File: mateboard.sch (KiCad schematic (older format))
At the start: 13 parts

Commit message: wifi bt leds
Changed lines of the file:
@@
 Connection ~ 8950 775
 Wire Wire Line
-	8475 775  8550 775
-Wire Wire Line
-	8550 775  8650 775
-Wire Wire Line
-	8650 775  8750 775
-Wire Wire Line
-	8750 775  8850 775
-Wire Wire Line
-	8850 775  8950 775
-Wire Wire Line
-	8950 775  9050 775
-Wire Wire Line
-	9050 775  9150 775
+	8475 775  9150 775
 Wire Wire Line
 	9050 775  9050 900
@@
 	9150 1200 9150 1250
 Wire Wire Line
-	8150 1250 9150 1250
-Wire Wire Line
-	9150 1250 9225 1250
-Wire Wire Line
-	8150 1350 9050 1350
-Wire Wire Line
-	9050 1350 9225 1350
+	8150 1250 9225 1250
+Wire Wire Line
+	8150 1350 9225 1350
 Wire Wire Line
 	9050 1350 9050 1200
 Wire Wire Line
-	8150 1450 8950 1450
-Wire Wire Line
-	8950 1450 9225 1450
+	8150 1450 9225 1450
 Wire Wire Line
 	8950 1450 8950 1200
@@
 	8550 1550 8550 775
 Wire Wire Line
-	8150 1650 8850 1650
-Wire Wire Line
-	8850 1650 9225 1650
+	8150 1650 9225 1650
 Wire Wire Line
 	8850 1650 8850 1200
@@
 $EndComp
 Wire Wire Line
-	9150 1750 9150 2200
-Wire Wire Line
-	9150 2200 9150 2250
+	9150 1750 9150 2250
 Wire Wire Line
 	9150 1750 9225 1750
 Wire Wire Line
-	8150 1850 8750 1850
-Wire Wire Line
-	8750 1850 9225 1850
+	8150 1850 9225 1850
 Wire Wire Line
 	8750 1850 8750 1200
 Wire Wire Line
-	8150 1950 8650 1950
-Wire Wire Line
-	8650 1950 9225 1950
+	8150 1950 9225 1950
 Wire Wire Line
 	8650 1950 8650 1200
@@
 Connection ~ 8550 775
 Wire Wire Line
-	8475 1200 8475 2100
-Wire Wire Line
-	8475 2100 8475 2850
+	8475 1200 8475 2850
 Wire Wire Line
 	9225 2200 9150 2200
@@
 	6500 2850 6275 2850
 Wire Wire Line
-	6275 2400 6275 2850
-Wire Wire Line
-	6275 2850 6275 4650
+	6275 2400 6275 4650
 Wire Wire Line
 	6275 2400 6125 2400

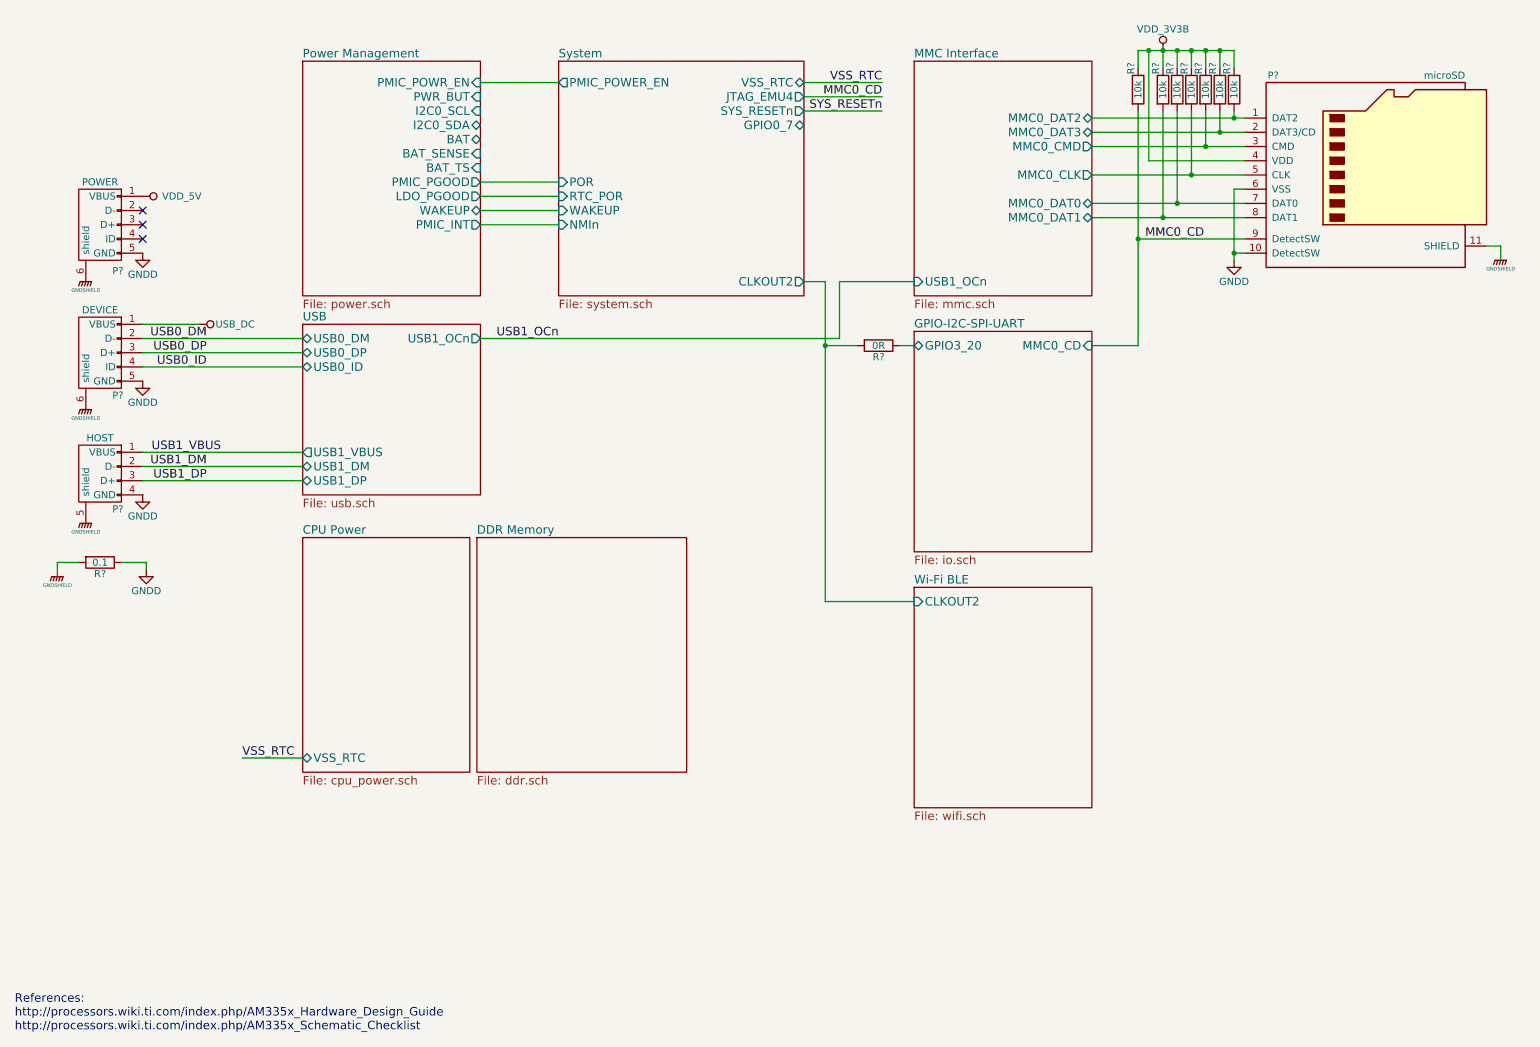
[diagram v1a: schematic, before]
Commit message: id eeprom
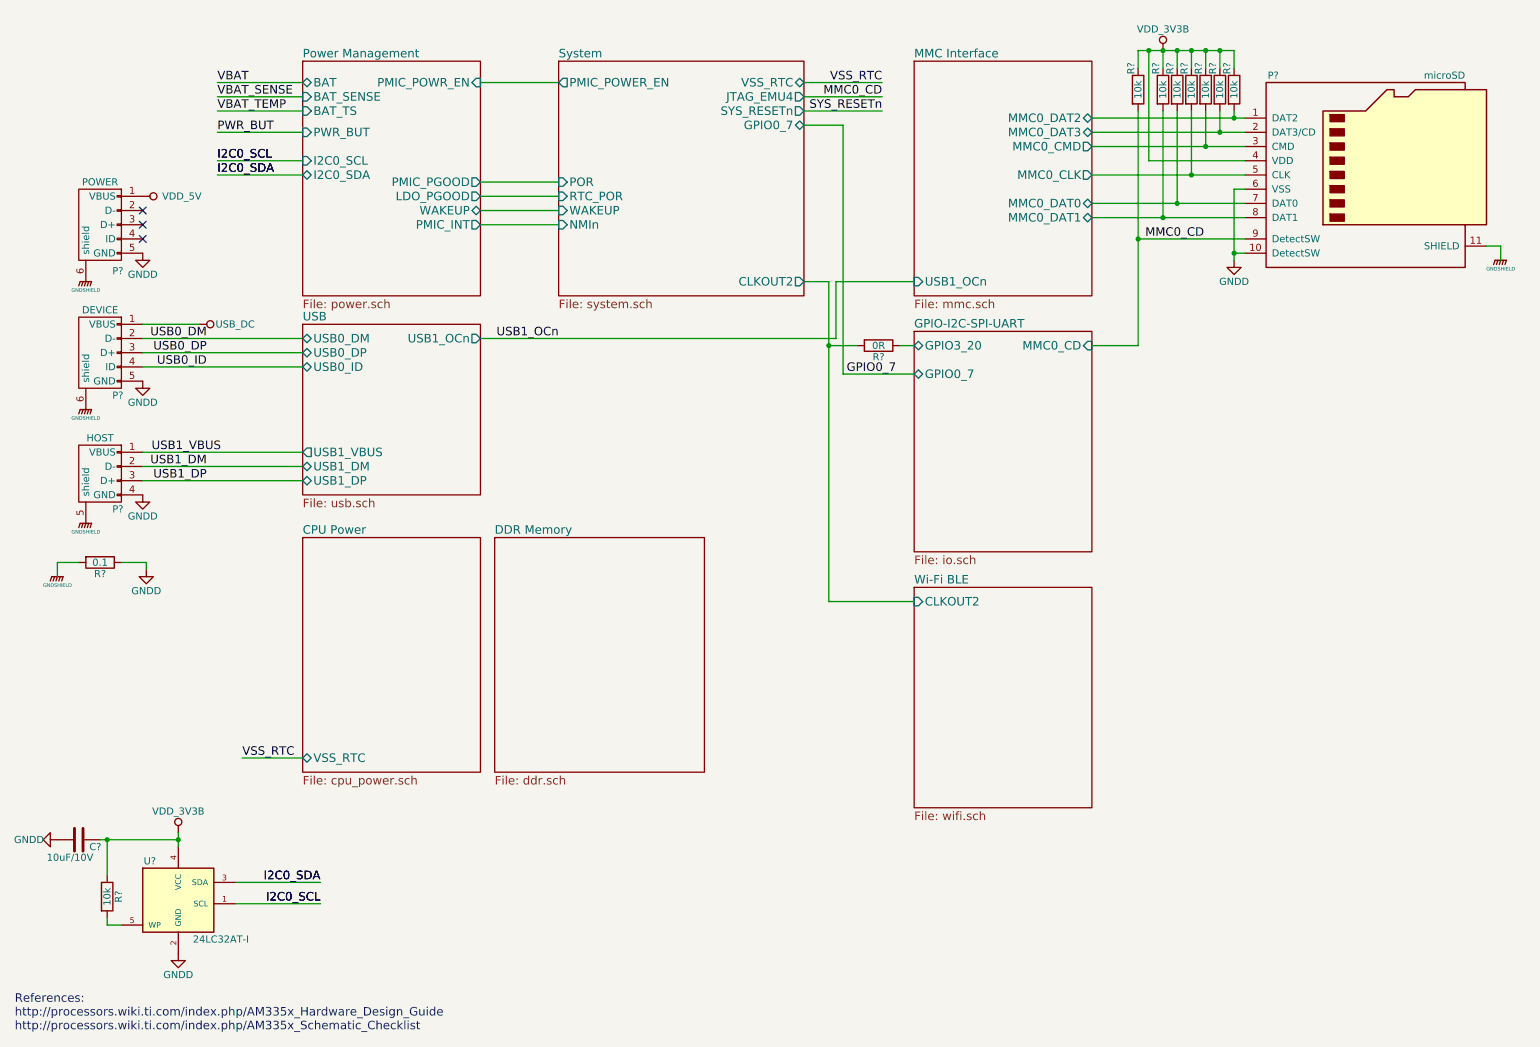
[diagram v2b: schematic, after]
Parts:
- added C?: 10uF/10V, symbol C
- added R?: 10k, symbol R
- added U?: 24LC32AT-I, TO_SOT_Packages_SMD:SOT-23-5, symbol AT24CS32-STUM
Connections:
- net GNDD: now also C?.2, U?.2 (GND)
- net VDD_3V3B: now also C?.1, R?.1, U?.4 (VCC)
- new net: R?.2, U?.5 (WP)
- new net I2C0_SCL: U?.1 (SCL)
- new net I2C0_SDA: U?.3 (SDA)
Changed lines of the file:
@@
 F1 "power.sch" 60
 F2 "PMIC_POWR_EN" I R 3850 1000 60
-F3 "PWR_BUT" I R 3850 1100 60
-F4 "I2C0_SCL" I R 3850 1200 60
-F5 "I2C0_SDA" B R 3850 1300 60
-F6 "BAT" B R 3850 1400 60
-F7 "BAT_SENSE" I R 3850 1500 60
-F8 "BAT_TS" I R 3850 1600 60
+F3 "PWR_BUT" I L 2600 1350 60
+F4 "I2C0_SCL" I L 2600 1550 60
+F5 "I2C0_SDA" B L 2600 1650 60
+F6 "BAT" B L 2600 1000 60
+F7 "BAT_SENSE" I L 2600 1100 60
+F8 "BAT_TS" I L 2600 1200 60
 F9 "PMIC_PGOOD" O R 3850 1700 60
 F10 "LDO_PGOOD" O R 3850 1800 60
@@
 $EndSheet
 $Sheet
-S 3825 4200 1475 1650
+S 3950 4200 1475 1650
 U 589C7F66
 F0 "DDR Memory" 60
@@
 F2 "MMC0_CD" I R 8150 2850 60
 F3 "GPIO3_20" B L 6900 2850 60
+F4 "GPIO0_7" B L 6900 3050 60
 $EndSheet
 $Comp
@@
 	1500 4375 1500 4425
 $Sheet
-S 2600 4200 1175 1650
+S 2600 4200 1250 1650
 U 589E2993
 F0 "CPU Power" 60
@@
 $EndComp
 Wire Wire Line
-	3850 2800 6375 2800
+	3850 2800 6350 2800
 Text Label 4400 2800 2    60   ~ 0
 USB1_OCn
 Wire Wire Line
-	6375 2400 6900 2400
+	6350 2400 6900 2400
 $Sheet
 S 6900 4550 1250 1550
@@
 $EndSheet
 Wire Wire Line
-	6375 2800 6375 2400
+	6350 2800 6350 2400
 Wire Wire Line
 	4400 2000 3850 2000
@@
 	6800 2850 6900 2850
 Wire Wire Line
-	6500 2850 6275 2850
-Wire Wire Line
-	6275 2400 6275 4650
-Wire Wire Line
-	6275 2400 6125 2400
-Wire Wire Line
-	6275 4650 6900 4650
-Connection ~ 6275 2850
+	6500 2850 6300 2850
+Wire Wire Line
+	6300 2400 6300 4650
+Wire Wire Line
+	6300 2400 6125 2400
+Wire Wire Line
+	6300 4650 6900 4650
+Connection ~ 6300 2850
+Wire Wire Line
+	6125 1300 6400 1300
+Wire Wire Line
+	6400 1300 6400 3050
+Wire Wire Line
+	6400 3050 6900 3050
+Text Label 6425 3050 0    60   ~ 0
+GPIO0_7
+Wire Wire Line
+	2600 1000 2000 1000
+Text Label 2000 1000 0    60   ~ 0
+VBAT
+Text Label 2000 1100 0    60   ~ 0
+VBAT_SENSE
+Wire Wire Line
+	2000 1100 2600 1100
+Wire Wire Line
+	2600 1200 2000 1200
+Text Label 2000 1200 0    60   ~ 0
+VBAT_TEMP
+Wire Wire Line
+	2600 1350 2000 1350
+Text Label 2000 1350 0    60   ~ 0
+PWR_BUT
+Wire Wire Line
+	2600 1550 2000 1550
+Wire Wire Line
+	2000 1650 2600 1650
+Text Label 2000 1650 0    60   ~ 0
+I2C0_SDA
+Text Label 2000 1550 0    60   ~ 0
+I2C0_SCL
+$Comp
+L AT24CS32-STUM U?
+U 1 1 58BAF6FC
+P 1725 6725
+F 0 "U?" H 1525 6975 50  0000 C CNN
+F 1 "24LC32AT-I" H 2025 6425 50  0000 C CNN
+F 2 "TO_SOT_Packages_SMD:SOT-23-5" H 1725 6725 50  0001 C CIN
+F 3 "" H 1725 6725 50  0001 C CNN
+	1    1725 6725
+	1    0    0    -1
+$EndComp
+$Comp
+L VDD_3V3B #PWR?
+U 1 1 58BAF78B
+P 1725 6275
+F 0 "#PWR?" H 1725 6125 50  0001 C CNN
+F 1 "VDD_3V3B" H 1725 6425 50  0000 C CNN
+F 2 "" H 1725 6275 50  0000 C CNN
+F 3 "" H 1725 6275 50  0000 C CNN
+	1    1725 6275
+	1    0    0    -1
+$EndComp
+$Comp
+L C C?
+U 1 1 58BB10E1
+P 1025 6325
+F 0 "C?" V 1075 6400 50  0000 L CNN
+F 1 "10uF/10V" V 1150 6100 50  0000 L CNN
+F 2 "" H 1063 6175 50  0000 C CNN
+F 3 "" H 1025 6325 50  0000 C CNN
+	1    1025 6325
+	0    1    1    0
+$EndComp
+$Comp
+L GNDD #PWR?
+U 1 1 58BB10E8
+P 875 6325
+F 0 "#PWR?" H 875 6075 50  0001 C CNN
+F 1 "GNDD" V 875 6125 50  0000 C CNN
+F 2 "" H 875 6325 50  0000 C CNN
+F 3 "" H 875 6325 50  0000 C CNN
+	1    875  6325
+	0    1    1    0
+$EndComp
+Wire Wire Line
+	1175 6325 1725 6325
+Wire Wire Line
+	1725 6275 1725 6375
+Connection ~ 1725 6325
+$Comp
+L R R?
+U 1 1 58BB16F3
+P 1225 6725
+F 0 "R?" V 1305 6725 50  0000 C CNN
+F 1 "10k" V 1225 6725 50  0000 C CNN
+F 2 "" V 1155 6725 50  0001 C CNN
+F 3 "" H 1225 6725 50  0001 C CNN
+	1    1225 6725
+	1    0    0    -1
+$EndComp
+Wire Wire Line
+	1225 6875 1225 6925
+Wire Wire Line
+	1225 6925 1325 6925
+Wire Wire Line
+	1225 6325 1225 6575
+Connection ~ 1225 6325
+$Comp
+L GNDD #PWR?
+U 1 1 58BB231C
+P 1725 7125
+F 0 "#PWR?" H 1725 6875 50  0001 C CNN
+F 1 "GNDD" H 1725 6975 50  0000 C CNN
+F 2 "" H 1725 7125 50  0000 C CNN
+F 3 "" H 1725 7125 50  0000 C CNN
+	1    1725 7125
+	1    0    0    -1
+$EndComp
+Text Label 2000 1650 0    60   ~ 0
+I2C0_SDA
+Text Label 2000 1550 0    60   ~ 0
+I2C0_SCL
+Wire Wire Line
+	2125 6775 2725 6775
+Wire Wire Line
+	2725 6625 2125 6625
+Text Label 2725 6625 2    60   ~ 0
+I2C0_SDA
+Text Label 2725 6775 2    60   ~ 0
+I2C0_SCL
+Text Label 2725 6625 2    60   ~ 0
+I2C0_SDA
+Text Label 2725 6775 2    60   ~ 0
+I2C0_SCL
 $EndSCHEMATC

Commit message: gpio and boot config
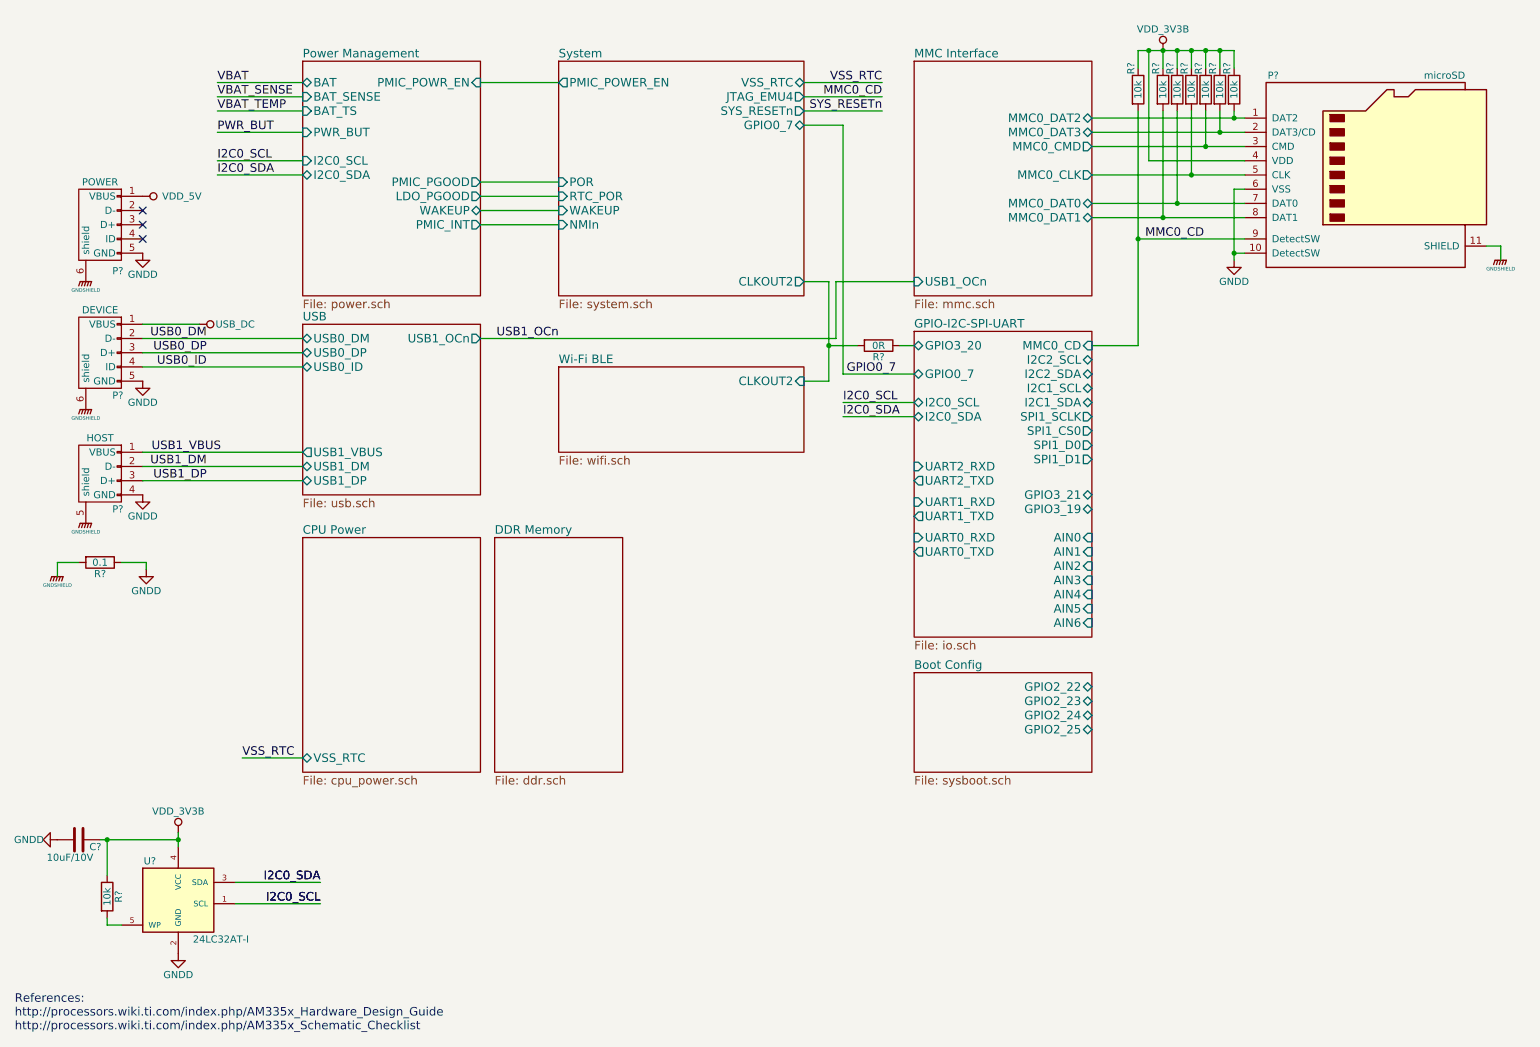
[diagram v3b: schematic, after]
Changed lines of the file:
@@
 $Descr A4 11693 8268
 encoding utf-8
-Sheet 1 9
+Sheet 1 10
 Title ""
 Date ""
@@
 $EndSheet
 $Sheet
-S 3950 4200 1475 1650
+S 3950 4200 900  1650
 U 589C7F66
 F0 "DDR Memory" 60
 F1 "ddr.sch" 60
-$EndSheet
-$Sheet
-S 6900 2750 1250 1550
-U 589C7F89
-F0 "GPIO-I2C-SPI-UART" 60
-F1 "io.sch" 60
-F2 "MMC0_CD" I R 8150 2850 60
-F3 "GPIO3_20" B L 6900 2850 60
-F4 "GPIO0_7" B L 6900 3050 60
 $EndSheet
 $Comp
@@
 Connection ~ 8950 775
 Wire Wire Line
-	8475 775  9150 775
+	8475 775  8550 775
+Wire Wire Line
+	8550 775  8650 775
+Wire Wire Line
+	8650 775  8750 775
+Wire Wire Line
+	8750 775  8850 775
+Wire Wire Line
+	8850 775  8950 775
+Wire Wire Line
+	8950 775  9050 775
+Wire Wire Line
+	9050 775  9150 775
 Wire Wire Line
 	9050 775  9050 900
@@
 	9150 1200 9150 1250
 Wire Wire Line
-	8150 1250 9225 1250
-Wire Wire Line
-	8150 1350 9225 1350
+	8150 1250 9150 1250
+Wire Wire Line
+	9150 1250 9225 1250
+Wire Wire Line
+	8150 1350 9050 1350
+Wire Wire Line
+	9050 1350 9225 1350
 Wire Wire Line
 	9050 1350 9050 1200
 Wire Wire Line
-	8150 1450 9225 1450
+	8150 1450 8950 1450
+Wire Wire Line
+	8950 1450 9225 1450
 Wire Wire Line
 	8950 1450 8950 1200
@@
 	8550 1550 8550 775
 Wire Wire Line
-	8150 1650 9225 1650
+	8150 1650 8850 1650
+Wire Wire Line
+	8850 1650 9225 1650
 Wire Wire Line
 	8850 1650 8850 1200
@@
 $EndComp
 Wire Wire Line
-	9150 1750 9150 2250
+	9150 1750 9150 2200
+Wire Wire Line
+	9150 2200 9150 2250
 Wire Wire Line
 	9150 1750 9225 1750
 Wire Wire Line
-	8150 1850 9225 1850
+	8150 1850 8750 1850
+Wire Wire Line
+	8750 1850 9225 1850
 Wire Wire Line
 	8750 1850 8750 1200
 Wire Wire Line
-	8150 1950 9225 1950
+	8150 1950 8650 1950
+Wire Wire Line
+	8650 1950 9225 1950
 Wire Wire Line
 	8650 1950 8650 1200
@@
 Connection ~ 8550 775
 Wire Wire Line
-	8475 1200 8475 2850
+	8475 1200 8475 2100
+Wire Wire Line
+	8475 2100 8475 2850
 Wire Wire Line
 	9225 2200 9150 2200
@@
 	6350 2400 6900 2400
 $Sheet
-S 6900 4550 1250 1550
+S 4400 3000 1725 600
 U 58AD6197
 F0 "Wi-Fi BLE" 60
 F1 "wifi.sch" 60
-F2 "CLKOUT2" I L 6900 4650 60
+F2 "CLKOUT2" I R 6125 3100 60
 $EndSheet
 Wire Wire Line
@@
 	6500 2850 6300 2850
 Wire Wire Line
-	6300 2400 6300 4650
+	6300 2400 6300 2850
+Wire Wire Line
+	6300 2850 6300 3100
 Wire Wire Line
 	6300 2400 6125 2400
-Wire Wire Line
-	6300 4650 6900 4650
 Connection ~ 6300 2850
 Wire Wire Line
@@
 Wire Wire Line
 	2000 1650 2600 1650
-Text Label 2000 1650 0    60   ~ 0
-I2C0_SDA
-Text Label 2000 1550 0    60   ~ 0
-I2C0_SCL
 $Comp
 L AT24CS32-STUM U?
@@
 $EndComp
 Wire Wire Line
-	1175 6325 1725 6325
-Wire Wire Line
-	1725 6275 1725 6375
+	1175 6325 1225 6325
+Wire Wire Line
+	1225 6325 1725 6325
+Wire Wire Line
+	1725 6275 1725 6325
+Wire Wire Line
+	1725 6325 1725 6375
 Connection ~ 1725 6325
 $Comp
@@
 Text Label 2725 6775 2    60   ~ 0
 I2C0_SCL
+Wire Wire Line
+	6900 3250 6400 3250
+Wire Wire Line
+	6400 3350 6900 3350
+Text Label 6400 3350 0    60   ~ 0
+I2C0_SDA
+Text Label 6400 3250 0    60   ~ 0
+I2C0_SCL
+$Sheet
+S 6900 5150 1250 700
+U 58BD360A
+F0 "Boot Config" 60
+F1 "sysboot.sch" 60
+F2 "GPIO2_23" B R 8150 5350 60
+F3 "GPIO2_22" B R 8150 5250 60
+F4 "GPIO2_24" B R 8150 5450 60
+F5 "GPIO2_25" B R 8150 5550 60
+$EndSheet
+Wire Wire Line
+	6300 3100 6125 3100
+$Sheet
+S 6900 2750 1250 2150
+U 589C7F89
+F0 "GPIO-I2C-SPI-UART" 60
+F1 "io.sch" 60
+F2 "MMC0_CD" I R 8150 2850 60
+F3 "GPIO3_20" B L 6900 2850 60
+F4 "GPIO0_7" B L 6900 3050 60
+F5 "I2C0_SCL" B L 6900 3250 60
+F6 "I2C0_SDA" B L 6900 3350 60
+F7 "I2C2_SCL" B R 8150 2950 60
+F8 "I2C2_SDA" B R 8150 3050 60
+F9 "I2C1_SCL" B R 8150 3150 60
+F10 "I2C1_SDA" B R 8150 3250 60
+F11 "AIN0" I R 8150 4200 60
+F12 "AIN1" I R 8150 4300 60
+F13 "AIN2" I R 8150 4400 60
+F14 "AIN3" I R 8150 4500 60
+F15 "AIN4" I R 8150 4600 60
+F16 "AIN5" I R 8150 4700 60
+F17 "AIN6" I R 8150 4800 60
+F18 "SPI1_SCLK" O R 8150 3350 60
+F19 "SPI1_CS0" O R 8150 3450 60
+F20 "SPI1_D0" O R 8150 3550 60
+F21 "GPIO3_21" B R 8150 3900 60
+F22 "GPIO3_19" B R 8150 4000 60
+F23 "SPI1_D1" O R 8150 3650 60
+F24 "UART2_RXD" I L 6900 3700 60
+F25 "UART2_TXD" O L 6900 3800 60
+F26 "UART1_RXD" I L 6900 3950 60
+F27 "UART1_TXD" O L 6900 4050 60
+F28 "UART0_RXD" I L 6900 4200 60
+F29 "UART0_TXD" O L 6900 4300 60
+$EndSheet
 $EndSCHEMATC
